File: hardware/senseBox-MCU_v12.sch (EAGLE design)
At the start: 140 parts, among them IC1 VREG-AP2111H-3V3, IC2 ATSAMD21G18A-MU, IC3 MAX8XX-809R, IC4 MAX8XX-809R, IC5 74LVC244PW, IC6 BMX055, IC7 ATECC608A-MAHDA, J1 USB-MICROB-2, J10 JST4-B4B-PH-SM4-TB, J11 JST4-B4B-PH-SM4-TB, J12 JST4-B4B-PH-SM4-TB, J13 JST4-B4B-PH-SM4-TB, J14 JUMPER3-0402, J15 JUMPER3-0402, J2 JST2-B2B-PH-SM4-TB, J3 SWD-2X5-SMD, J4 JST4-B4B-PH-SM4-TB, J5 JST4-B4B-PH-SM4-TB, J6 JST4-B4B-PH-SM4-TB, J7 JST4-B4B-PH-SM4-TB, J8 JST4-B4B-PH-SM4-TB, J9 JST4-B4B-PH-SM4-TB, Q1 32.768KHz, SW1 PTS645SH50SMTR92-Grey, SW2 PTS645SK50SMTR92-Red, T1 BSS138PS, T2 P-Chn, T3 P-Chn, T4 P-Chn, T5 BSS138PS, T6 BSS138PS, T7 P-Chn, X1 PASSER-07, X2 PASSER-07, X3 PASSER-07, X4 PASSER-07

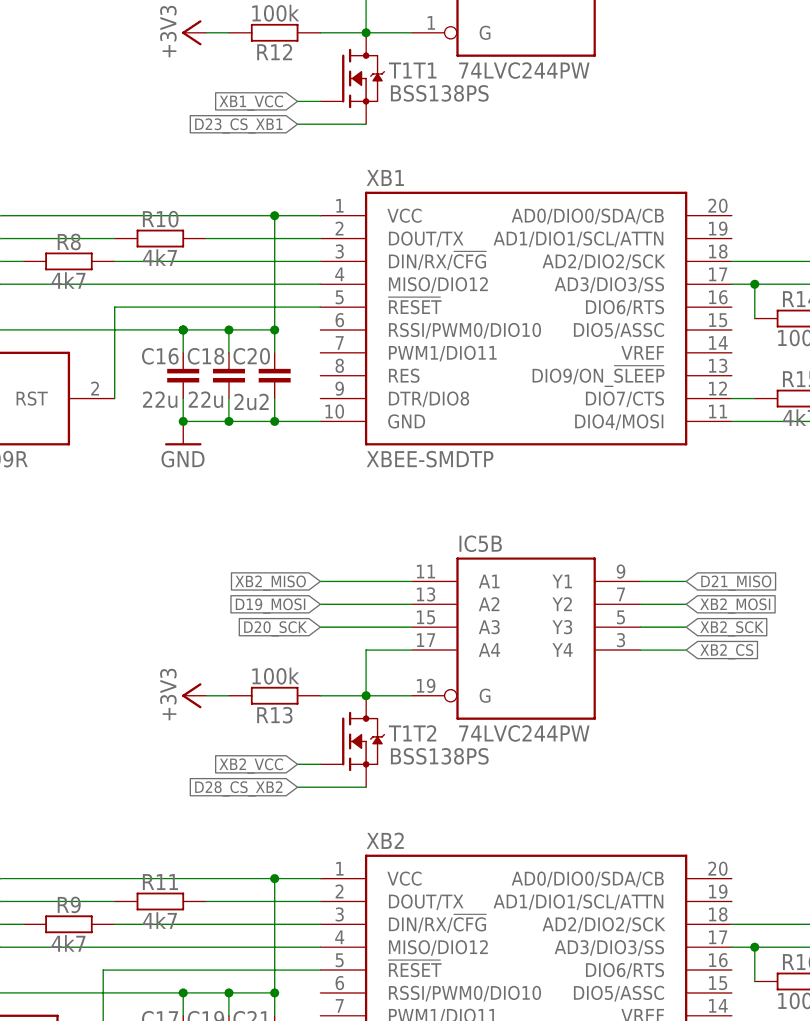
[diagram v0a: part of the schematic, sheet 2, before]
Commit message: updated schematics
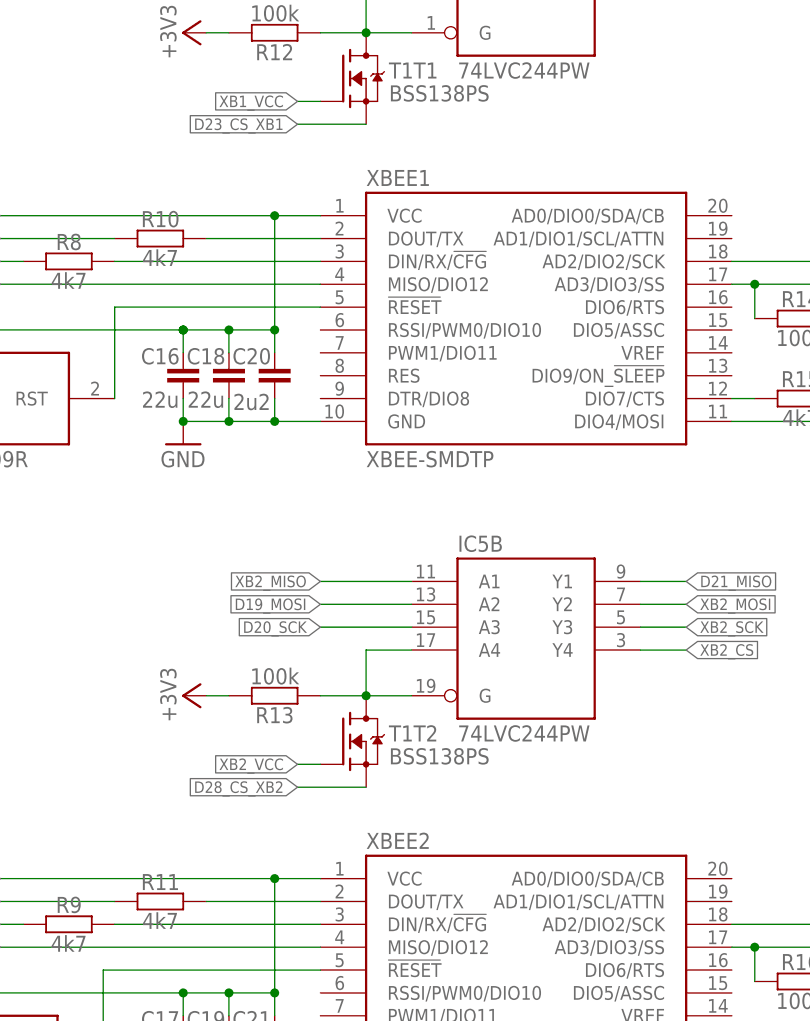
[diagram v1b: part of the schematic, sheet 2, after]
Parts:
- renumbered XB1 to XBEE1, XB2 to XBEE2
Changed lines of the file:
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@@
 <part name="FRAME1" library="we-symbol" deviceset="FRAME-A4L" device=""/>
 <part name="LOGO3" library="we-symbol" deviceset="LOGO_OSHW" device="-3" value="OSHW_LOGOX0070"/>
-<part name="XB1" library="we-board" deviceset="XBEE" device="-SMDTP" value="XBEE-SMDTP"/>
+<part name="XBEE1" library="we-board" deviceset="XBEE" device="-SMDTP" value="XBEE-SMDTP"/>
 <part name="X4" library="we-symbol" deviceset="PASSER" device="-07"/>
 <part name="C20" library="we-rcl" deviceset="CAPACITOR" device="-0402" value="2u2"/>
@@
 <part name="C18" library="we-rcl" deviceset="CAPACITOR" device="-0805" value="22u"/>
 <part name="C16" library="we-rcl" deviceset="CAPACITOR" device="-0805" value="22u"/>
-<part name="XB2" library="we-board" deviceset="XBEE" device="-SMDTP" value="XBEE-SMDTP"/>
+<part name="XBEE2" library="we-board" deviceset="XBEE" device="-SMDTP" value="XBEE-SMDTP"/>
 <part name="C21" library="we-rcl" deviceset="CAPACITOR" device="-0402" value="2u2"/>
 <part name="C19" library="we-rcl" deviceset="CAPACITOR" device="-0805" value="22u"/>
@@
 </plain>
 <instances>
-<instance part="XB1" gate="BOARD" x="107.95" y="115.57"/>
+<instance part="XBEE1" gate="BOARD" x="107.95" y="115.57"/>
 <instance part="C20" gate="C" x="80.01" y="107.95" smashed="yes" rot="R90">
 <attribute name="NAME" x="77.47" y="109.22" size="1.778" layer="95" align="bottom-center"/>
@@
 <attribute name="VALUE" x="67.31" y="106.172" size="1.778" layer="96" align="top-center"/>
 </instance>
-<instance part="XB2" gate="BOARD" x="107.95" y="41.91"/>
+<instance part="XBEE2" gate="BOARD" x="107.95" y="41.91"/>
 <instance part="C21" gate="C" x="80.01" y="34.29" smashed="yes" rot="R90">
 <attribute name="NAME" x="77.47" y="35.56" size="1.778" layer="95" align="bottom-center"/>
@@
 <net name="GND" class="0">
 <segment>
-<pinref part="XB1" gate="BOARD" pin="GND"/>
+<pinref part="XBEE1" gate="BOARD" pin="GND"/>
 <pinref part="C20" gate="C" pin="1"/>
 <wire x1="85.09" y1="102.87" x2="80.01" y2="102.87" width="0.1524" layer="91"/>
@@
 </segment>
 <segment>
-<pinref part="XB2" gate="BOARD" pin="GND"/>
+<pinref part="XBEE2" gate="BOARD" pin="GND"/>
 <pinref part="C21" gate="C" pin="1"/>
 <wire x1="85.09" y1="29.21" x2="80.01" y2="29.21" width="0.1524" layer="91"/>
@@
 <net name="XB1_TX" class="0">
 <segment>
-<pinref part="XB1" gate="BOARD" pin="DOUT/TX"/>
+<pinref part="XBEE1" gate="BOARD" pin="DOUT/TX"/>
 <pinref part="R10" gate="R" pin="2"/>
 <wire x1="72.39" y1="123.19" x2="85.09" y2="123.19" width="0.1524" layer="91"/>
@@
 <wire x1="146.05" y1="118.11" x2="133.35" y2="118.11" width="0.1524" layer="91"/>
 <label x="146.05" y="118.11" size="1.27" layer="95" xref="yes"/>
-<pinref part="XB1" gate="BOARD" pin="AD3/DIO3/SS"/>
+<pinref part="XBEE1" gate="BOARD" pin="AD3/DIO3/SS"/>
 <pinref part="R14" gate="R" pin="1"/>
 <wire x1="133.35" y1="118.11" x2="130.81" y2="118.11" width="0.1524" layer="91"/>
@@
 <wire x1="49.53" y1="118.11" x2="85.09" y2="118.11" width="0.1524" layer="91"/>
 <label x="49.53" y="118.11" size="1.27" layer="95" rot="R180" xref="yes"/>
-<pinref part="XB1" gate="BOARD" pin="MISO/DIO12"/>
+<pinref part="XBEE1" gate="BOARD" pin="MISO/DIO12"/>
 </segment>
 <segment>
@@
 <wire x1="146.05" y1="102.87" x2="130.81" y2="102.87" width="0.1524" layer="91"/>
 <label x="146.05" y="102.87" size="1.27" layer="95" xref="yes"/>
-<pinref part="XB1" gate="BOARD" pin="DIO4/MOSI"/>
+<pinref part="XBEE1" gate="BOARD" pin="DIO4/MOSI"/>
 </segment>
 <segment>
@@
 <wire x1="146.05" y1="120.65" x2="130.81" y2="120.65" width="0.1524" layer="91"/>
 <label x="146.05" y="120.65" size="1.27" layer="95" xref="yes"/>
-<pinref part="XB1" gate="BOARD" pin="AD2/DIO2/SCK"/>
+<pinref part="XBEE1" gate="BOARD" pin="AD2/DIO2/SCK"/>
 </segment>
 <segment>
@@
 <segment>
 <wire x1="133.35" y1="105.41" x2="130.81" y2="105.41" width="0.1524" layer="91"/>
-<pinref part="XB1" gate="BOARD" pin="DIO7/CTS"/>
+<pinref part="XBEE1" gate="BOARD" pin="DIO7/CTS"/>
 <pinref part="R15" gate="R" pin="1"/>
 </segment>
@@
 <net name="XB1_VCC" class="0">
 <segment>
-<pinref part="XB1" gate="BOARD" pin="VCC"/>
+<pinref part="XBEE1" gate="BOARD" pin="VCC"/>
 <label x="49.53" y="125.73" size="1.27" layer="95" rot="R180" xref="yes"/>
 <wire x1="85.09" y1="125.73" x2="80.01" y2="125.73" width="0.1524" layer="91"/>
@@
 <net name="XB1_RX" class="0">
 <segment>
-<pinref part="XB1" gate="BOARD" pin="DIN/RX/!CFG!"/>
+<pinref part="XBEE1" gate="BOARD" pin="DIN/RX/!CFG!"/>
 <pinref part="R8" gate="R" pin="2"/>
 <wire x1="85.09" y1="120.65" x2="62.23" y2="120.65" width="0.1524" layer="91"/>
@@
 <net name="XB2_VCC" class="0">
 <segment>
-<pinref part="XB2" gate="BOARD" pin="VCC"/>
+<pinref part="XBEE2" gate="BOARD" pin="VCC"/>
 <label x="49.53" y="52.07" size="1.27" layer="95" rot="R180" xref="yes"/>
 <pinref part="C17" gate="C" pin="2"/>
@@
 <net name="XB2_TX" class="0">
 <segment>
-<pinref part="XB2" gate="BOARD" pin="DOUT/TX"/>
+<pinref part="XBEE2" gate="BOARD" pin="DOUT/TX"/>
 <pinref part="R11" gate="R" pin="2"/>
 <wire x1="72.39" y1="49.53" x2="85.09" y2="49.53" width="0.1524" layer="91"/>
@@
 <net name="XB2_RX" class="0">
 <segment>
-<pinref part="XB2" gate="BOARD" pin="DIN/RX/!CFG!"/>
+<pinref part="XBEE2" gate="BOARD" pin="DIN/RX/!CFG!"/>
 <pinref part="R9" gate="R" pin="2"/>
 <wire x1="62.23" y1="46.99" x2="85.09" y2="46.99" width="0.1524" layer="91"/>
@@
 <wire x1="49.53" y1="44.45" x2="85.09" y2="44.45" width="0.1524" layer="91"/>
 <label x="49.53" y="44.45" size="1.27" layer="95" rot="R180" xref="yes"/>
-<pinref part="XB2" gate="BOARD" pin="MISO/DIO12"/>
+<pinref part="XBEE2" gate="BOARD" pin="MISO/DIO12"/>
 </segment>
 <segment>
@@
 <wire x1="146.05" y1="46.99" x2="130.81" y2="46.99" width="0.1524" layer="91"/>
 <label x="146.05" y="46.99" size="1.27" layer="95" xref="yes"/>
-<pinref part="XB2" gate="BOARD" pin="AD2/DIO2/SCK"/>
+<pinref part="XBEE2" gate="BOARD" pin="AD2/DIO2/SCK"/>
 </segment>
 <segment>
@@
 <wire x1="146.05" y1="44.45" x2="133.35" y2="44.45" width="0.1524" layer="91"/>
 <label x="146.05" y="44.45" size="1.27" layer="95" xref="yes"/>
-<pinref part="XB2" gate="BOARD" pin="AD3/DIO3/SS"/>
+<pinref part="XBEE2" gate="BOARD" pin="AD3/DIO3/SS"/>
 <pinref part="R16" gate="R" pin="1"/>
 <wire x1="133.35" y1="44.45" x2="130.81" y2="44.45" width="0.1524" layer="91"/>
@@
 <segment>
 <wire x1="133.35" y1="31.75" x2="130.81" y2="31.75" width="0.1524" layer="91"/>
-<pinref part="XB2" gate="BOARD" pin="DIO7/CTS"/>
+<pinref part="XBEE2" gate="BOARD" pin="DIO7/CTS"/>
 <pinref part="R17" gate="R" pin="1"/>
 </segment>
@@
 <wire x1="146.05" y1="29.21" x2="130.81" y2="29.21" width="0.1524" layer="91"/>
 <label x="146.05" y="29.21" size="1.27" layer="95" xref="yes"/>
-<pinref part="XB2" gate="BOARD" pin="DIO4/MOSI"/>
+<pinref part="XBEE2" gate="BOARD" pin="DIO4/MOSI"/>
 </segment>
 <segment>
@@
 <net name="RST_XB1" class="0">
 <segment>
-<pinref part="XB1" gate="BOARD" pin="!RESET!"/>
+<pinref part="XBEE1" gate="BOARD" pin="!RESET!"/>
 <pinref part="IC4" gate="IC" pin="RST"/>
 <wire x1="85.09" y1="115.57" x2="62.23" y2="115.57" width="0.1524" layer="91"/>
@@
 <net name="RST_XB2" class="0">
 <segment>
-<pinref part="XB2" gate="BOARD" pin="!RESET!"/>
+<pinref part="XBEE2" gate="BOARD" pin="!RESET!"/>
 <pinref part="IC3" gate="IC" pin="RST"/>
 <wire x1="85.09" y1="41.91" x2="60.96" y2="41.91" width="0.1524" layer="91"/>
